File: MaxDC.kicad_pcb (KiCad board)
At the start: 2 copper layers, 100 x 100 mm, 34 parts, among them J1 L N E, J2 Screw_Terminal_01x04, T2 70063K

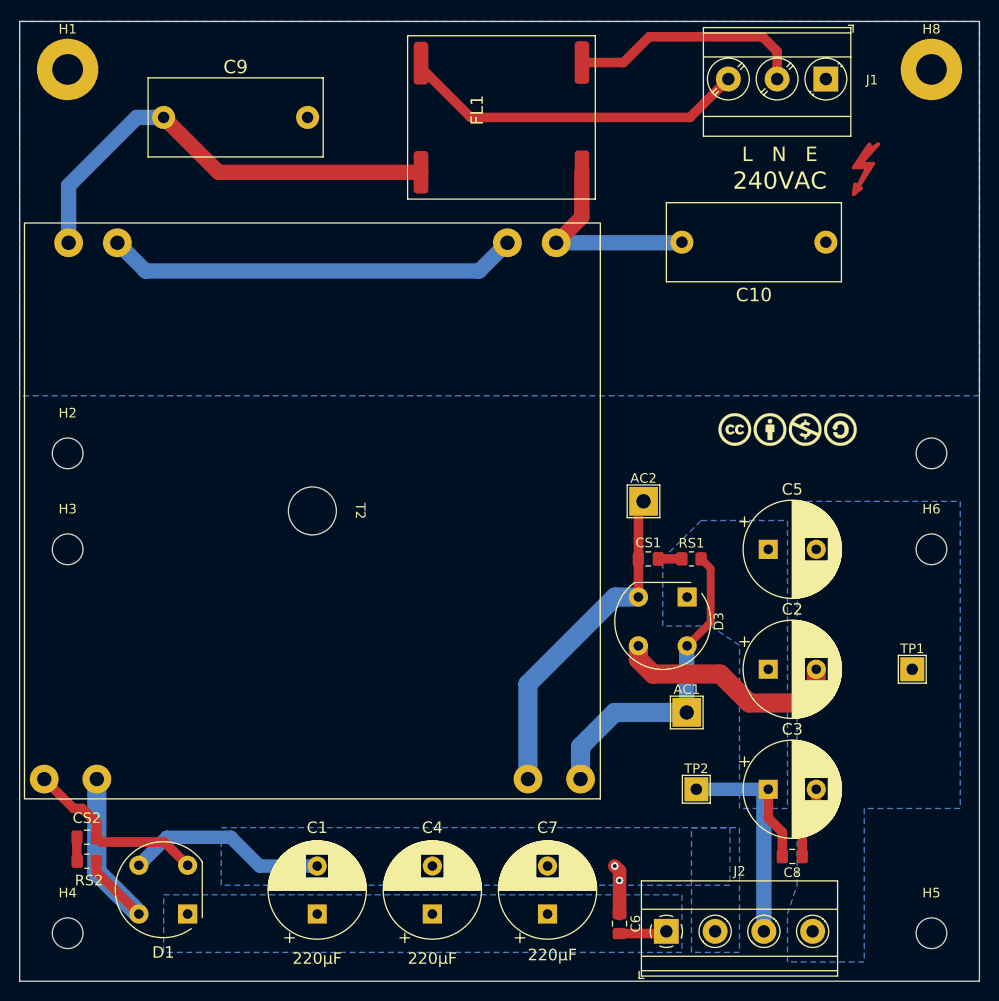
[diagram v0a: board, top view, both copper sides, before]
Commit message: Add files via upload
Rev 0.3 adjusts the board layout to fit inside a Hammond 1455 series enclosure.    Move components and line voltage traces in from the edges of the PCB.
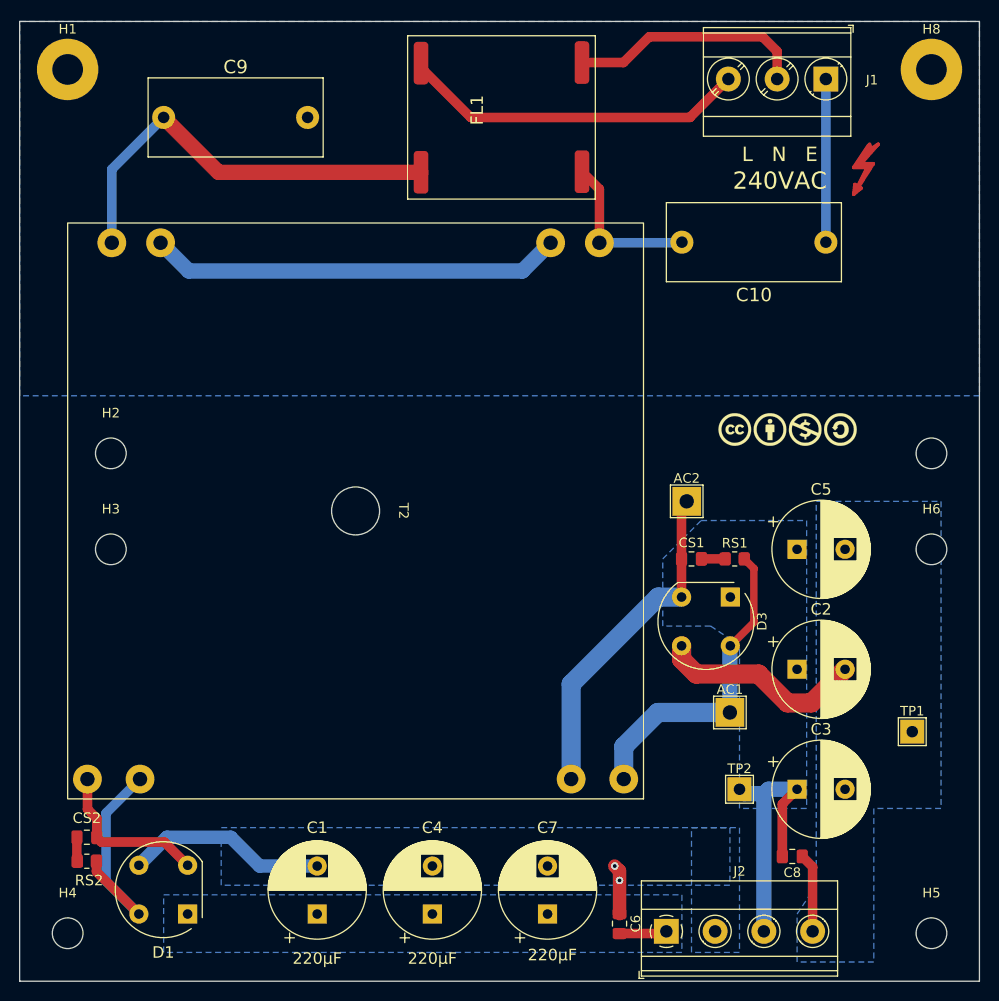
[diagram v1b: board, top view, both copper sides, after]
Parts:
- moved TP1 6.50 mm to (193.0, 124.0)
- moved AC1 4.50 mm to (174.0, 122.0)
- moved AC2 4.50 mm to (169.5, 100.0)
- moved CS1 4.50 mm to (170.0, 106.0)
- moved D3 4.50 mm to (174.0, 110.0)
- moved H2 4.50 mm to (109.5, 95.0)
- moved H3 4.50 mm to (109.5, 105.0)
- moved RS1 4.50 mm to (174.5, 106.0)
- moved T2 4.50 mm to (135.0, 101.0)
- moved TP2 4.50 mm to (175.0, 130.0)
- moved C2 3.00 mm to (181.0, 117.5)
- moved C3 3.00 mm to (181.0, 130.0)
- moved C5 3.00 mm to (181.0, 105.0)
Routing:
- net Earth_Protective: track 0.00 -> 17.0 mm
- net Net-(C10-Pad2): track 21.6 -> 16.8 mm
- net Net-(C9-Pad1): track 48.0 -> 44.5 mm
- net Net-(CS2-Pad1): track 19.5 -> 17.2 mm
- net T3: track 30.1 -> 28.4 mm
- net T4: track 31.8 -> 30.0 mm
- net Net-(D1-Pad4): track 23.2 -> 24.3 mm
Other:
- board text added: "MaxDC 0.3 Andrew Fischer 26012023 License: Creative Commons CC BY-NC 4.0 creativecommons.org/licenses/by-nc/4.0/"
- board text removed: "MaxDC 0.2 Andrew Fischer 24012023 License: Creative Commons CC BY-NC 4.0 creativecommons.org/licenses/by-nc/4.0/"

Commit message: Add files via upload
28012023 Uploaded to JLCPCB
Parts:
- moved 240VAC 4.09 mm to (188.0, 70.0)
- moved AC1 4.00 mm to (174.0, 118.0)
- moved AC2 4.00 mm to (169.5, 96.0)
- moved C10 4.00 mm to (184.0, 77.0)
- moved C2 4.00 mm to (181.0, 113.5)
- moved C3 4.00 mm to (181.0, 126.0)
- moved C5 4.00 mm to (181.0, 101.0)
- moved CS1 4.00 mm to (170.0, 102.0)
- moved D3 4.00 mm to (174.0, 106.0)
- moved J1 4.00 mm to (184.0, 60.0)
- moved RS1 4.00 mm to (174.5, 102.0)
- moved TP1 4.00 mm to (193.0, 120.0)
- moved TP2 4.00 mm to (175.0, 126.0)
- moved C8 3.81 mm to (180.5, 133.2)
- moved J2 3.81 mm to (167.4, 141.0)
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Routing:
- net T1: track 4.98 -> 19.8 mm
- net Net-(AC2-Pad1): track 35.4 -> 37.9 mm
- net Net-(AC1-Pad1): track 33.4 -> 35.3 mm
- net Net-(FL1-Pad4): track 25.0 -> 26.7 mm
- net Net-(FL1-Pad1): track 36.3 -> 34.6 mm
- net Net-(C10-Pad2): track 16.8 -> 18.4 mm
- net T3: track 28.4 -> 29.5 mm
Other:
- board size 100 x 100 mm -> 99.5 x 100 mm
- board text added: "+"
- board text added: "-"
- board text added: "MaxDC 0.3 Andrew Fischer 28012023 License: Creative Commons CC BY-NC 4.0 creativecommons.org/licenses/by-nc/4.0/"
- board text removed: "MaxDC 0.3 Andrew Fischer 26012023 License: Creative Commons CC BY-NC 4.0 creativecommons.org/licenses/by-nc/4.0/"
